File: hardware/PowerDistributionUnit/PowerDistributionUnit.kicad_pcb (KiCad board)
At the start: 2 copper layers, 99.1 x 60.2 mm, 101 parts, among them J1 973582101, J2 973582100, J3 973582101, J4 973582100, Q1 SQJ141ELP, Q2 CSD18511Q5A, SW1 SW_Push, U1 TPS25983, U2 AD5258, U3 NUCLEO_L432KC

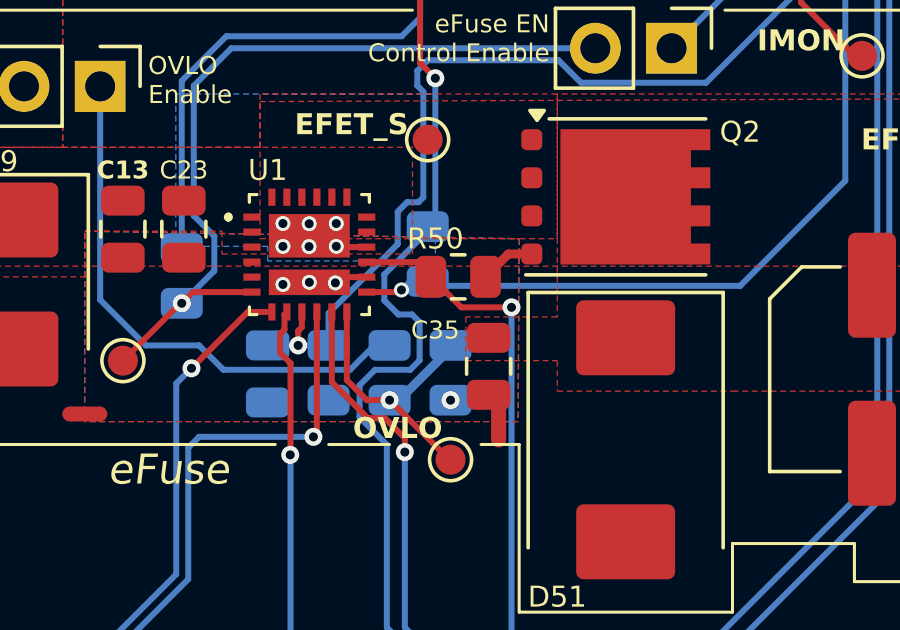
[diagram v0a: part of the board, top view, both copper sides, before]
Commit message: removed third net tie for eFuse GND island, adjusted routing to tie two halves of GND island together
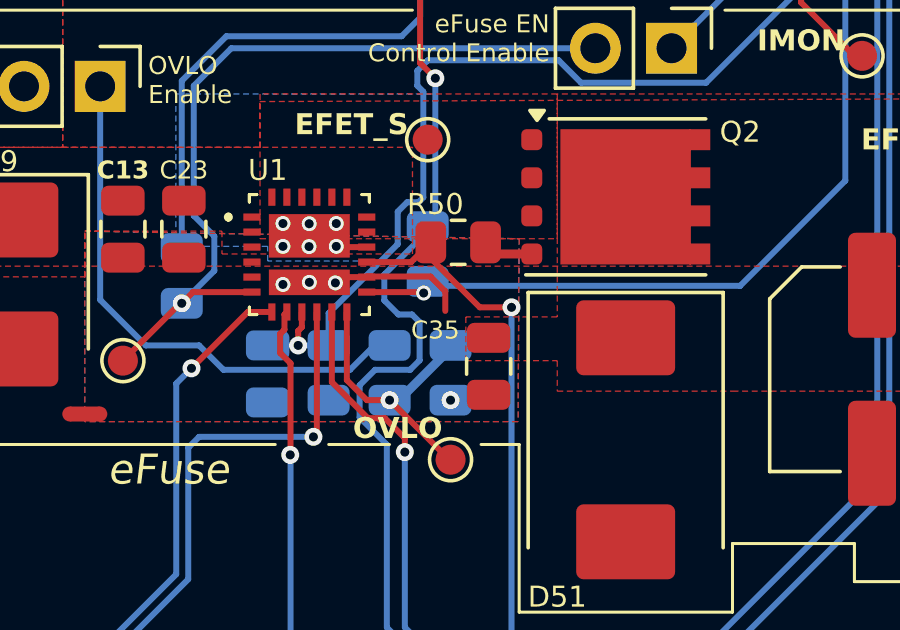
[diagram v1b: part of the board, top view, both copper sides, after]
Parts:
- removed NT3: NetTie_2, NetTie:NetTie-2_SMD_Pad0.5mm
- moved R50 1.15 mm to (134.0, 99.6)
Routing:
- net GND: track 10.5 -> 14.0 mm
- net /dVdt/BGATE: track 49.8 -> 50.7 mm
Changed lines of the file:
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@@
 		)
 	)
-	(footprint "NetTie:NetTie-2_SMD_Pad0.5mm"
-		(layer "F.Cu")
-		(at 135.382 105.656 90)
-		(descr "Net tie, 2 pin, 0.5mm square SMD pads")
-		(tags "net tie")
-		(property "Reference" "NT3"
-			(at 0 -1.2 90)
-			(layer "F.SilkS")
-			(hide yes)
-			(effects
-				(font
-					(size 1 1)
-					(thickness 0.15)
-				)
-			)
-		)
-		(property "Value" "NetTie_2"
-			(at 0 1.2 90)
-			(layer "F.Fab")
-			(hide yes)
-			(effects
-				(font
-					(size 1 1)
-					(thickness 0.15)
-				)
-			)
-		)
-		(property "Footprint" "NetTie:NetTie-2_SMD_Pad0.5mm"
-			(at 0 0 90)
-			(unlocked yes)
-			(layer "F.Fab")
-			(hide yes)
-			(effects
-				(font
-					(size 1.27 1.27)
-					(thickness 0.15)
-				)
-			)
-		)
-		(property "Datasheet" ""
-			(at 0 0 90)
-			(unlocked yes)
-			(layer "F.Fab")
-			(hide yes)
-			(effects
-				(font
-					(size 1.27 1.27)
-					(thickness 0.15)
-				)
-			)
-		)
-		(property "Description" "Net tie, 2 pins"
-			(at 0 0 90)
-			(unlocked yes)
-			(layer "F.Fab")
-			(hide yes)
-			(effects
-				(font
-					(size 1.27 1.27)
-					(thickness 0.15)
-				)
-			)
-		)
-		(property ki_fp_filters "Net*Tie*")
-		(sheetname "Root")
-		(sheetfile "PowerDistributionUnit.kicad_sch")
-		(attr exclude_from_pos_files exclude_from_bom allow_missing_courtyard)
-		(net_tie_pad_groups "1, 2")
-		(fp_poly
-			(pts
-				(xy -0.5 -0.25) (xy 0.5 -0.25) (xy 0.5 0.25) (xy -0.5 0.25)
-			)
-			(stroke
-				(width 0)
-				(type solid)
-			)
-			(fill solid)
-			(layer "F.Cu")
-		)
-		(pad "1" smd circle
-			(at -0.5 0 90)
-			(size 0.5 0.5)
-			(layers "F.Cu")
-			(net 18 "GNDPWR")
-			(pinfunction "1")
-			(pintype "passive")
-		)
-		(pad "2" smd circle
-			(at 0.5 0 90)
-			(size 0.5 0.5)
-			(layers "F.Cu")
-			(net 1 "GND")
-			(pinfunction "2")
-			(pintype "passive")
-		)
-	)
 	(footprint "Diode_SMD:D_SOD-323"
 		(layer "F.Cu")
@@
 	(footprint "Resistor_SMD:R_0805_2012Metric"
 		(layer "F.Cu")
-		(at 134.034 100.718 180)
+		(at 134.034 99.568 180)
 		(descr "Resistor SMD 0805 (2012 Metric), square (rectangular) end terminal, IPC_7351 nominal, (Body size source: IPC-SM-782 page 72, https://www.pcb-3d.com/wordpress/wp-content/uploads/ipc-sm-782a_amendment_1_and_2.pdf), generated with kicad-footprint-generator")
 		(tags "resistor")
@@
 	)
 	(segment
+		(start 130.986 100.726)
+		(end 131.004194 100.707806)
+		(width 0.2)
+		(layer "F.Cu")
+		(net 1)
+	)
+	(segment
 		(start 111.936 78.154)
 		(end 111.936 78.553999)
@@
 	)
 	(segment
+		(start 131.004194 100.707806)
+		(end 133.111305 100.707806)
+		(width 0.2)
+		(layer "F.Cu")
+		(net 1)
+	)
+	(segment
 		(start 129.073 100.901)
 		(end 129.248 100.726)
@@
 	)
 	(segment
+		(start 133.604 101.200501)
+		(end 133.604 101.854)
+		(width 0.2)
+		(layer "F.Cu")
+		(net 1)
+	)
+	(segment
 		(start 111.936 78.553999)
 		(end 112.236001 78.854)
@@
 	)
 	(segment
+		(start 133.111305 100.707806)
+		(end 133.604 101.200501)
+		(width 0.2)
+		(layer "F.Cu")
+		(net 1)
+	)
+	(segment
 		(start 113.46 78.316596)
 		(end 113.46 77.858)
@@
 	)
 	(segment
+		(start 133.1215 99.568)
+		(end 132.4635 100.226)
+		(width 0.2)
+		(layer "F.Cu")
+		(net 30)
+	)
+	(segment
 		(start 161.015 117.981)
 		(end 159.382 117.981)
@@
 	)
 	(segment
-		(start 162.04 119.006)
-		(end 161.015 117.981)
+		(start 132.4635 100.226)
+		(end 130.986 100.226)
 		(width 0.2)
 		(layer "F.Cu")
@@
 	)
 	(segment
-		(start 157.402 116.974)
-		(end 156.386 116.974)
+		(start 162.04 119.006)
+		(end 161.015 117.981)
 		(width 0.2)
 		(layer "F.Cu")
@@
 	(segment
 		(start 157.402 116.974)
-		(end 157.402 118.051)
+		(end 156.386 116.974)
 		(width 0.2)
 		(layer "F.Cu")
@@
 	)
 	(segment
-		(start 154.74 119.006)
-		(end 156.386 117.36)
+		(start 157.402 116.974)
+		(end 157.402 118.051)
 		(width 0.2)
 		(layer "F.Cu")
@@
 	)
 	(segment
-		(start 132.6295 100.226)
-		(end 130.986 100.226)
+		(start 134.754 101.734)
+		(end 133.1215 100.1015)
 		(width 0.2)
 		(layer "F.Cu")
@@
 	)
 	(segment
-		(start 133.1215 100.718)
-		(end 132.6295 100.226)
+		(start 133.1215 100.1015)
+		(end 133.1215 99.568)
 		(width 0.2)
 		(layer "F.Cu")
@@
 	)
 	(segment
-		(start 159.382 117.981)
-		(end 158.357 119.006)
+		(start 135.812 101.734)
+		(end 134.754 101.734)
 		(width 0.2)
 		(layer "F.Cu")
@@
 	)
 	(segment
-		(start 156.386 117.36)
-		(end 156.386 116.974)
+		(start 154.74 119.006)
+		(end 156.386 117.36)
 		(width 0.2)
 		(layer "F.Cu")
@@
 	)
 	(segment
-		(start 135.812 101.734)
-		(end 134.1375 101.734)
+		(start 159.382 117.981)
+		(end 158.357 119.006)
 		(width 0.2)
 		(layer "F.Cu")
@@
 	)
 	(segment
-		(start 134.1375 101.734)
-		(end 133.1215 100.718)
+		(start 156.386 117.36)
+		(end 156.386 116.974)
 		(width 0.2)
 		(layer "F.Cu")
@@
 	)
 	(segment
-		(start 136.4865 99.956)
-		(end 135.7085 99.956)
+		(start 135.0805 99.956)
+		(end 134.9465 99.822)
 		(width 0.3)
 		(layer "F.Cu")
@@
 	)
 	(segment
-		(start 135.7085 99.956)
-		(end 134.9465 100.718)
+		(start 136.4865 99.956)
+		(end 135.0805 99.956)
 		(width 0.3)
 		(layer "F.Cu")
@@
 	)
 	(segment
-		(start 132.072 101.226)
-		(end 130.986 101.226)
+		(start 155.624 91.828)
+		(end 155.624 89.034)
 		(width 0.2)
 		(layer "F.Cu")
@@
 	)
 	(segment
-		(start 155.624 91.828)
-		(end 155.624 89.034)
+		(start 132.883487 101.257806)
+		(end 132.851681 101.226)
 		(width 0.2)
 		(layer "F.Cu")
@@
 	)
 	(segment
-		(start 132.143 101.155)
-		(end 132.072 101.226)
+		(start 132.851681 101.226)
+		(end 130.986 101.226)
 		(width 0.2)
 		(layer "F.Cu")
@@
 	)
 	(via
-		(at 132.143 101.155)
+		(at 132.883487 101.257806)
 		(size 0.5)
 		(drill 0.3)
@@
 	)
 	(segment
-		(start 132.143 101.155)
-		(end 132.4295 100.8685)
+		(start 132.883487 101.257806)
+		(end 132.883487 101.003013)
 		(width 0.2)
 		(layer "B.Cu")
@@
 	)
 	(segment
-		(start 143.432 101.019)
-		(end 146.939 97.512)
+		(start 132.883487 101.003013)
+		(end 133.018 100.8685)
 		(width 0.2)
 		(layer "B.Cu")
@@
 	)
 	(segment
-		(start 154.159 87.569)
-		(end 155.624 89.034)
+		(start 143.432 101.019)
+		(end 146.939 97.512)
 		(width 0.2)
 		(layer "B.Cu")
@@
 	)
 	(segment
-		(start 132.4295 100.8685)
-		(end 133.018 100.8685)
+		(start 154.159 87.569)
+		(end 155.624 89.034)
 		(width 0.2)
 		(layer "B.Cu")

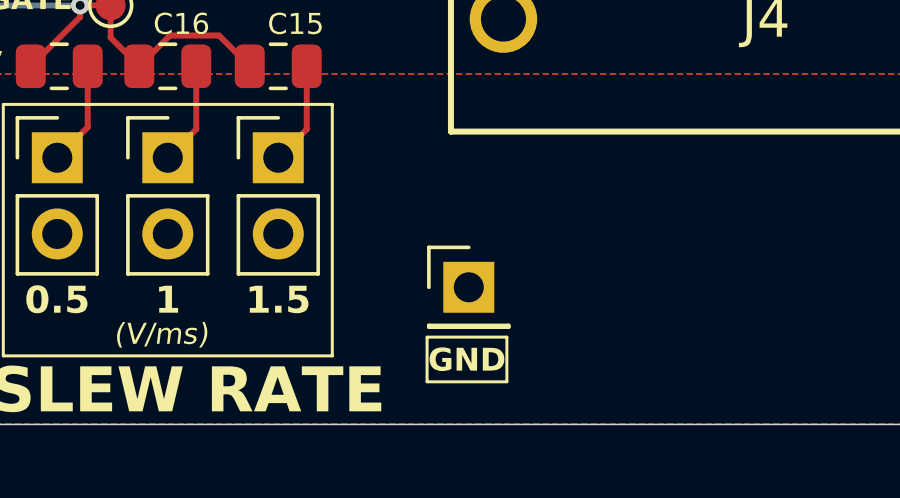
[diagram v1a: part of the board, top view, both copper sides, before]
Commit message: added silkscreen board name and human names
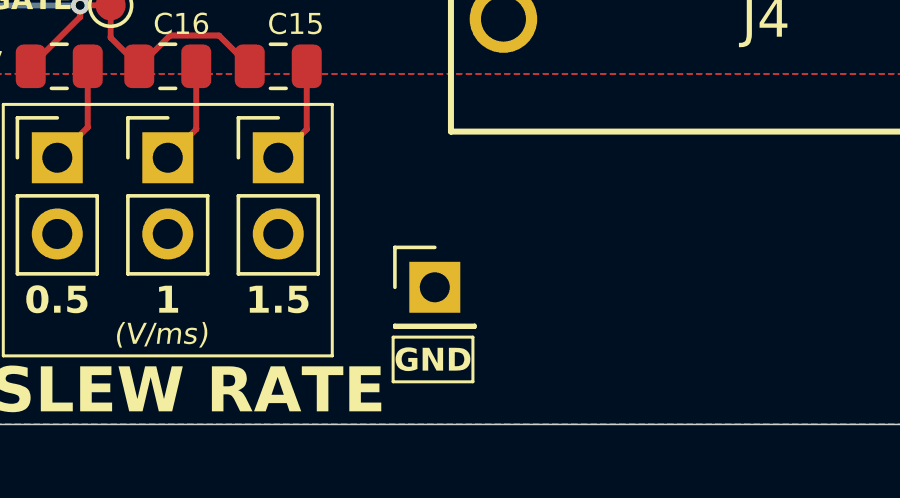
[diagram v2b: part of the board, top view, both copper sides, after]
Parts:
- added G***: LOGO, LOGO, B.Cu at (178.1, 80.5)
- moved TP6 1.13 mm to (168.2, 126.4)
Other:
- board text added: "Changxu Liu"
- board text added: "Wataru Yasueda"
- board text added: "eFuse Test Board"
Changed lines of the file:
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@@
 	(footprint "Connector_PinHeader_2.54mm:PinHeader_1x01_P2.54mm_Vertical"
 		(layer "F.Cu")
-		(at 169.34 126.372)
+		(at 168.208 126.372)
 		(descr "Through hole straight pin header, 1x01, 2.54mm pitch, single row")
 		(tags "Through hole pin header THT 1x01 2.54mm single row")
@@
 		)
 	)
+	(footprint "LOGO"
+		(layer "B.Cu")
+		(at 178.054 80.518 180)
+		(property "Reference" "G***"
+			(at 2.286 -8.128 0)
+			(layer "B.SilkS")
+			(hide yes)
+			(effects
+				(font
+					(size 1.5 1.5)
+					(thickness 0.3)
+				)
+				(justify mirror)
+			)
+		)
+		(property "Value" "LOGO"
+			(at 0.75 0 0)
+			(layer "B.SilkS")
+			(hide yes)
+			(effects
+				(font
+					(size 1.5 1.5)
+					(thickness 0.3)
+				)
+				(justify mirror)
+			)
+		)
+		(property "Footprint" ""
+			(at 0 0 0)
+			(layer "B.Fab")
+			(hide yes)
+			(effects
+				(font
+					(size 1.27 1.27)
+					(thickness 0.15)
+				)
+				(justify mirror)
+			)
+		)
+		(property "Datasheet" ""
+			(at 0 0 0)
+			(layer "B.Fab")
+			(hide yes)
+			(effects
+				(font
+					(size 1.27 1.27)
+					(thickness 0.15)
+				)
+				(justify mirror)
+			)
+		)
+		(property "Description" ""
+			(at 0 0 0)
+			(layer "B.Fab")
+			(hide yes)
+			(effects
+				(font
+					(size 1.27 1.27)
+					(thickness 0.15)
+				)
+				(justify mirror)
+			)
+		)
+		(attr board_only exclude_from_pos_files exclude_from_bom)
+		(fp_poly
+			(pts
+				(xy -6.249206 0.201587) (xy -6.224007 -0.932341) (xy -5.203472 -0.945984) (xy -4.182936 -0.959627)
+				(xy -4.182936 -1.210567) (xy -4.182936 -1.461508) (xy -5.519249 -1.461508) (xy -6.855562 -1.461508)
+				(xy -6.842166 -0.062996) (xy -6.828769 1.335516) (xy -6.551587 1.335516) (xy -6.274404 1.335516)
+			)
+			(stroke
+				(width 0)
+				(type solid)
+			)
+			(fill solid)
+			(layer "B.SilkS")
+		)
+		(fp_poly
+			(pts
+				(xy 6.853969 0.831548) (xy 6.853969 0.604762) (xy 6.072818 0.604762) (xy 5.291667 0.604762) (xy 5.291667 0.352778)
+				(xy 5.291667 0.100794) (xy 6.072818 0.100794) (xy 6.853969 0.100794) (xy 6.853969 -0.604762) (xy 6.853969 -1.310317)
+				(xy 5.846032 -1.310317) (xy 4.838096 -1.310317) (xy 4.838096 -1.083532) (xy 4.838096 -0.856746)
+				(xy 5.619247 -0.856746) (xy 6.400397 -0.856746) (xy 6.400397 -0.604762) (xy 6.400397 -0.352778)
+				(xy 5.619247 -0.352778) (xy 4.838096 -0.352778) (xy 4.838096 0.352778) (xy 4.838096 1.058333) (xy 5.846032 1.058333)
+				(xy 6.853969 1.058333)
+			)
+			(stroke
+				(width 0)
+				(type solid)
+			)
+			(fill solid)
+			(layer "B.SilkS")
+		)
+		(fp_poly
+			(pts
+				(xy -0.373172 1.351622) (xy -0.176388 1.335516) (xy -0.162992 -0.062996) (xy -0.149596 -1.461508)
+				(xy -0.476322 -1.461508) (xy -0.803048 -1.461508) (xy -0.817297 -0.894544) (xy -0.831547 -0.327579)
+				(xy -1.926018 -0.314002) (xy -3.02049 -0.300424) (xy -3.034749 -0.868367) (xy -3.049007 -1.436309)
+				(xy -3.364789 -1.451334) (xy -3.680571 -1.466359) (xy -3.66717 -0.065422) (xy -3.653769 1.335516)
+				(xy -3.397309 1.350467) (xy -3.19821 1.345631) (xy -3.089637 1.303072) (xy -3.084272 1.297248) (xy -3.058725 1.219919)
+				(xy -3.035949 1.067249) (xy -3.019124 0.864691) (xy -3.013153 0.727931) (xy -2.998611 0.226786)
+				(xy -1.915079 0.226786) (xy -0.831547 0.226786) (xy -0.817248 0.768018) (xy -0.807939 1.025937)
+				(xy -0.788229 1.198713) (xy -0.746219 1.301983) (xy -0.67001 1.351387) (xy -0.547702 1.362562)
+			)
+			(stroke
+				(width 0)
+				(type solid)
+			)
+			(fill solid)
+			(layer "B.SilkS")
+		)
+		(fp_poly
+			(pts
+				(xy 1.856389 1.355612) (xy 2.179517 1.351768) (xy 2.647725 1.343299) (xy 3.025655 1.330623) (xy 3.323823 1.309636)
+				(xy 3.552744 1.276235) (xy 3.722934 1.226314) (xy 3.844908 1.155771) (xy 3.929182 1.0605) (xy 3.986272 0.936398)
+				(xy 4.026693 0.77936) (xy 4.055352 0.619636) (xy 4.065781 0.417178) (xy 4.042188 0.194687) (xy 3.991695 -0.013856)
+				(xy 3.921422 -0.174474) (xy 3.877371 -0.229668) (xy 3.81313 -0.295584) (xy 3.813297 -0.34789) (xy 3.880288 -0.42808)
+				(xy 3.889499 -0.437893) (xy 3.945563 -0.512859) (xy 3.98223 -0.610283) (xy 4.005316 -0.755142) (xy 4.020634 -0.972413)
+				(xy 4.022438 -1.008937) (xy 4.044076 -1.461508) (xy 3.710332 -1.461508) (xy 3.376588 -1.461508)
+				(xy 3.376588 -1.165923) (xy 3.364342 -0.959221) (xy 3.321898 -0.815859) (xy 3.272136 -0.73755) (xy 3.167685 -0.604762)
+				(xy 2.213803 -0.604762) (xy 1.259921 -0.604762) (xy 1.259921 -1.033135) (xy 1.259921 -1.461508)
+				(xy 0.932342 -1.461508) (xy 0.604762 -1.461508) (xy 0.604762 -0.076555) (xy 0.604762 0.386376) (xy 1.259921 0.386376)
+				(xy 1.264188 0.188839) (xy 1.275542 0.031118) (xy 1.291816 -0.06052) (xy 1.297719 -0.071607) (xy 1.357819 -0.082707)
+				(xy 1.502244 -0.090712) (xy 1.714564 -0.095269) (xy 1.978345 -0.096027) (xy 2.277158 -0.092634)
+				(xy 2.278719 -0.092606) (xy 2.615482 -0.085515) (xy 2.865965 -0.077118) (xy 3.044681 -0.065912)
+				(xy 3.166141 -0.050393) (xy 3.244859 -0.029059) (xy 3.295349 -0.000405) (xy 3.311853 0.014399) (xy 3.377195 0.13253)
+				(xy 3.401407 0.323995) (xy 3.401786 0.35903) (xy 3.391791 0.528363) (xy 3.35341 0.635296) (xy 3.28281 0.710008)
+				(xy 3.23272 0.743946) (xy 3.168423 0.768891) (xy 3.074814 0.786205) (xy 2.936788 0.797245) (xy 2.73924 0.803369)
+				(xy 2.467064 0.805938) (xy 2.211878 0.806349) (xy 1.259921 0.806349) (xy 1.259921 0.386376) (xy 0.604762 0.386376)
+				(xy 0.604762 1.308397) (xy 0.730608 1.339983) (xy 0.813764 1.347766) (xy 0.982805 1.353342) (xy 1.222847 1.356589)
+				(xy 1.519004 1.357386)
+			)
+			(stroke
+				(width 0)
+				(type solid)
+			)
+			(fill solid)
+			(layer "B.SilkS")
+		)
+	)
 	(footprint "Resistor_SMD:R_0805_2012Metric"
 		(layer "B.Cu")
@@
 		)
 	)
+	(gr_circle
+		(center 164.846 84.328)
+		(end 165.04713 84.328)
+		(stroke
+			(width 0.1)
+			(type solid)
+		)
+		(fill solid)
+		(layer "B.SilkS")
+	)
 	(gr_line
 		(start 116.508 106.306)
@@
 	)
 	(gr_rect
-		(start 167.95 128.0333)
-		(end 170.61 129.5227)
+		(start 166.818 128.0333)
+		(end 169.478 129.5227)
 		(stroke
 			(width 0.1)
@@
 		(layer "Edge.Cuts")
 	)
+	(gr_text "eFuse Test Board"
+		(at 169.418 82.042 0)
+		(layer "B.SilkS")
+		(effects
+			(font
+				(size 2 2)
+				(thickness 0.3)
+				(bold yes)
+			)
+			(justify left bottom mirror)
+		)
+	)
+	(gr_text "Wataru Yasueda"
+		(at 164.084 84.836 -0)
+		(layer "B.SilkS")
+		(effects
+			(font
+				(size 1 1)
+				(thickness 0.1)
+			)
+			(justify left bottom mirror)
+		)
+	)
+	(gr_text "Changxu Liu"
+		(at 175.006 84.836 -0)
+		(layer "B.SilkS")
+		(effects
+			(font
+				(size 1 1)
+				(thickness 0.1)
+			)
+			(justify left bottom mirror)
+		)
+	)
 	(gr_text "+3V3"
 		(at 122.096 76.08 0)
@@
 	)
 	(gr_text "GND"
-		(at 169.28 129.2433 0)
+		(at 168.148 129.2433 0)
 		(layer "F.SilkS" knockout)
 		(effects
